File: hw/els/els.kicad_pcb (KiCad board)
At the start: 2 copper layers, 150 x 114.9 mm, 51 parts, among them J1 Conn_01x02, J10 Conn_01x02, J11 Conn_01x02, J12 LCD, J13 KEYPAD, J14 INPUT ENCODER, J15 SPINDLE ENCODER, J16 Z STEPPER, J17 X STEPPER, J18 USB_B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

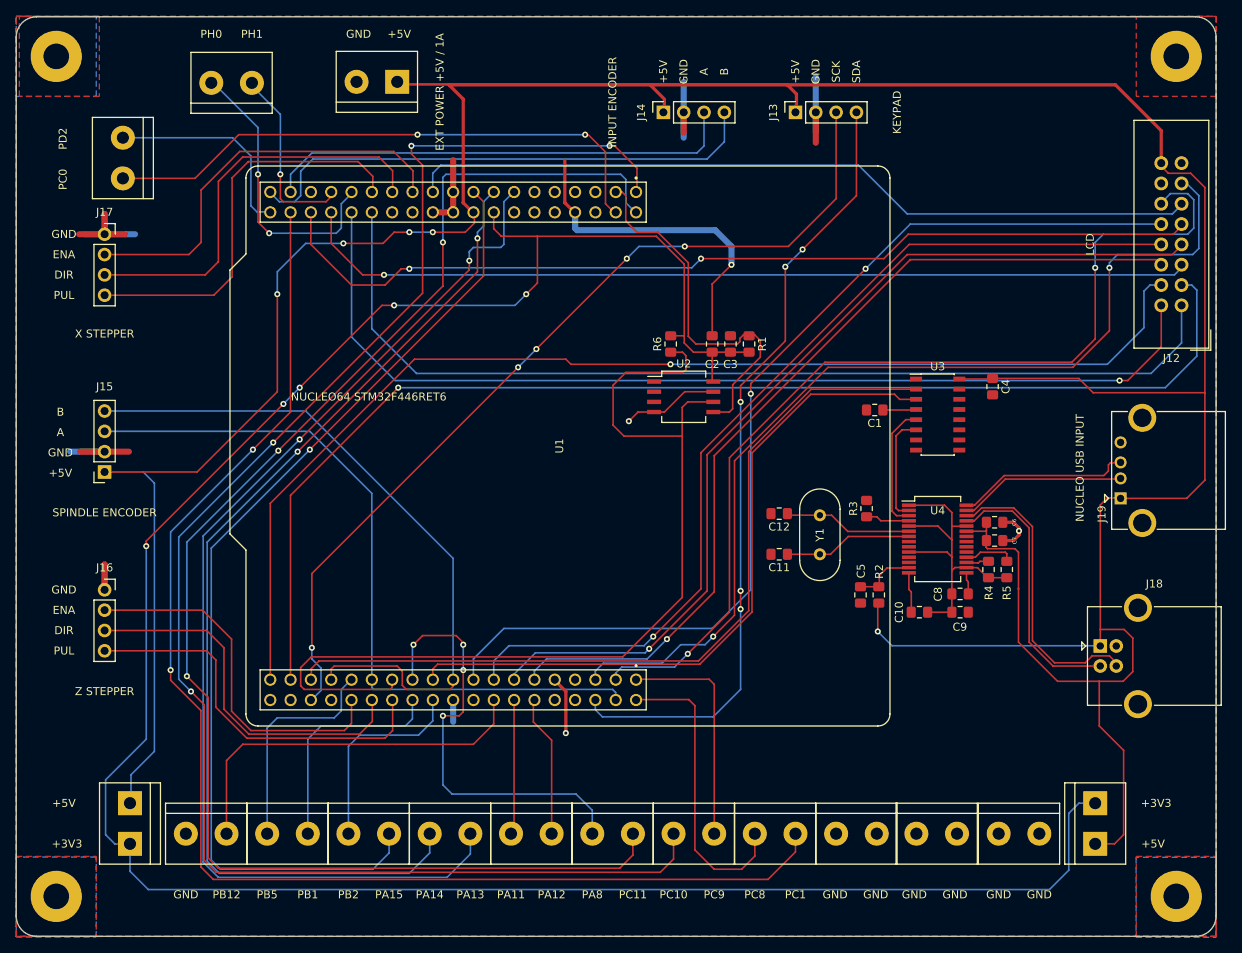
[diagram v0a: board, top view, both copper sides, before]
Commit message: Initial migration of els Kicad files to Kicad 6.0
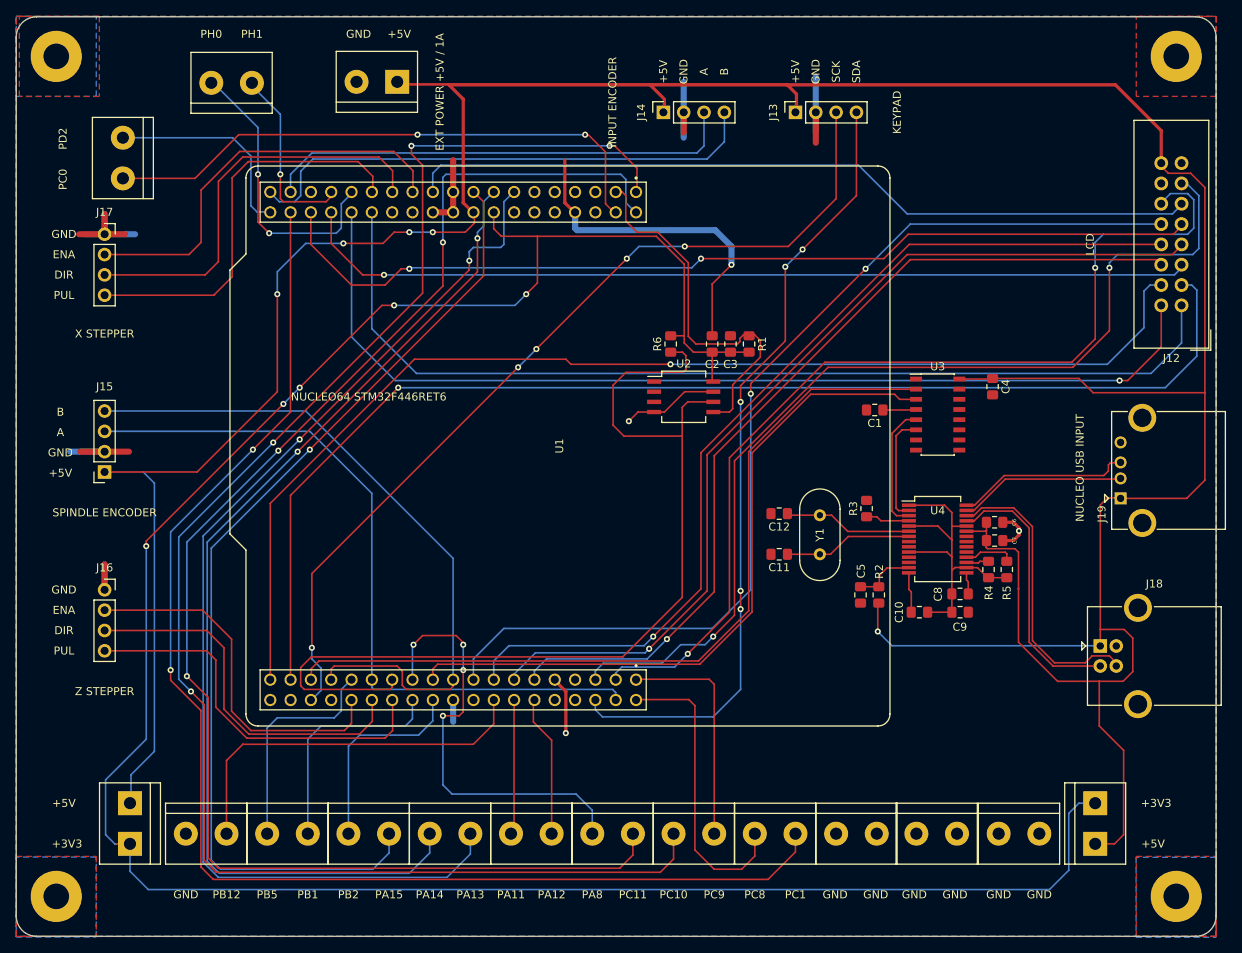
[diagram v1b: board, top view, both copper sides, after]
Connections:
- net ~RST renamed ~{RST}
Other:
- net class Default removed
